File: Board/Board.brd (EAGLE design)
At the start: 99 x 99 mm, 108 parts, among them IC1 7805TV, IC2 LM358D, IC3 MCP23S17SO, IC4 ATMEGA328P_TQFP, IC5 MAX232SOIC16, IC6 MCP4921, IC7 TL431CD, IC8 DS18B20, IC9 DS18B20, Q1 IRF3710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

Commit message: renamed Board Files in preparation for Exporting PDFs
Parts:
- KK1, KK3: value SK104-PAD -> SK104
- KK2: value SK95-2M3 -> SK95
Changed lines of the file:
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@@
 <attribute name="VALUE" x="63.627" y="55.245" size="1.27" layer="27" rot="R90"/>
 </element>
-<element name="KK1" library="heatsink" package="SK104-PAD" value="SK104-PAD" x="91.44" y="68.58" smashed="yes" rot="R270">
+<element name="KK1" library="heatsink" package="SK104-PAD" value="SK104" x="91.44" y="68.58" smashed="yes" rot="R270">
 <attribute name="VALUE" x="84.963" y="75.184" size="1.778" layer="27" ratio="10" rot="R270"/>
 </element>
@@
 <attribute name="VALUE" x="30.48" y="49.53" size="0.4064" layer="27" rot="R180"/>
 </element>
-<element name="KK2" library="heatsink" package="SK95-2M3" value="SK95-2M3" x="6.35" y="71.12" smashed="yes" rot="R90">
+<element name="KK2" library="heatsink" package="SK95-2M3" value="SK95" x="6.35" y="71.12" smashed="yes" rot="R90">
 <attribute name="VALUE" x="0.635" y="71.12" size="1.27" layer="27" ratio="10" rot="R90"/>
 </element>
@@
 <element name="JP3" library="SparkFun-Connectors" package="MOLEX-1X4" value="" x="63.5" y="92.44" rot="MR270"/>
 <element name="JP4" library="SparkFun-Connectors" package="MOLEX-1X4" value="" x="25.4" y="57.15"/>
-<element name="KK3" library="heatsink" package="SK104-PAD" value="SK104-PAD" x="91.44" y="29.21" smashed="yes" rot="R270">
+<element name="KK3" library="heatsink" package="SK104-PAD" value="SK104" x="91.44" y="29.21" smashed="yes" rot="R270">
 <attribute name="VALUE" x="84.963" y="35.814" size="1.778" layer="27" ratio="10" rot="R270"/>
 </element>

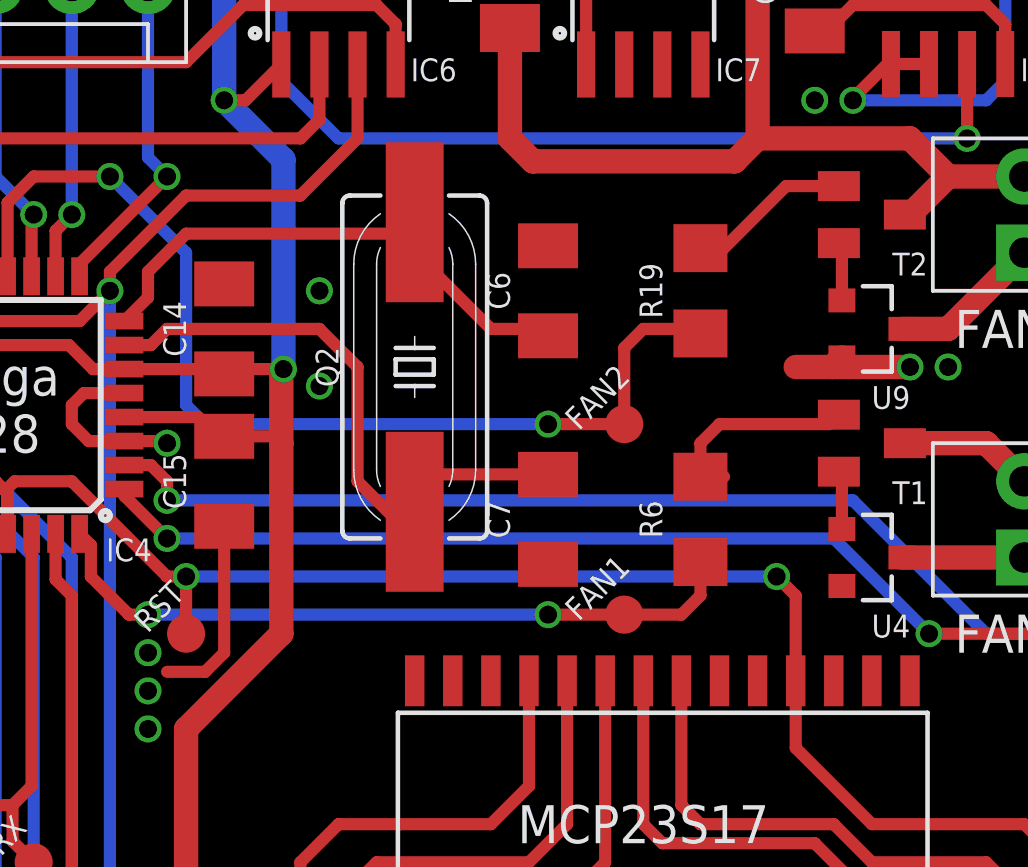
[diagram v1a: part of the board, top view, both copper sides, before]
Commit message: added pull downs to fan drver gates
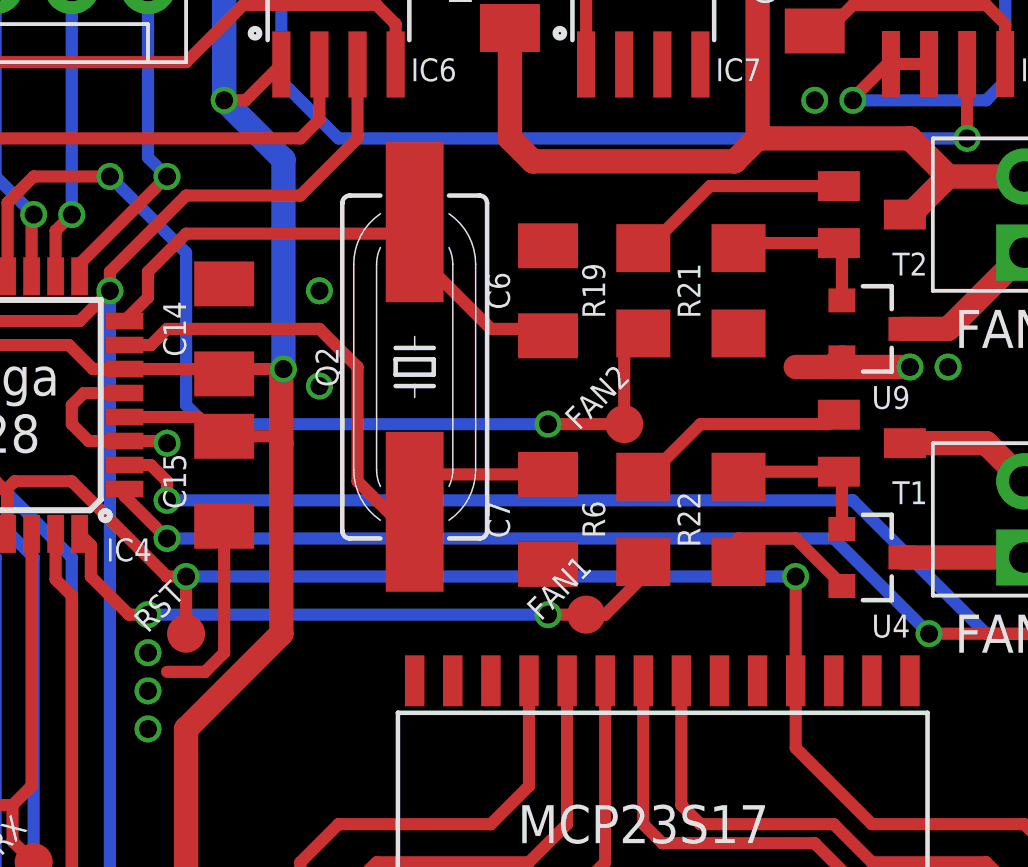
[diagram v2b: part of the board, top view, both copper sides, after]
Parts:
- added R21, R22: 10k, rcl:R1206
- moved R19 1.91 mm to (49.5, 47.0)
- moved R6 1.91 mm to (49.5, 39.4)
- moved FAN1 1.27 mm to (47.6, 36.2)
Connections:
- net GND: now also R21.2, R22.2
- net N$4: now also R22.1
- net N$42: now also R21.1
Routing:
- net GND: track 49.9 -> 54.8 mm
- net N$42: track 1.95 -> 5.37 mm
- net N$4: track 1.95 -> 5.37 mm
- net N$48: track 5.60 -> 8.60 mm
- net FAN1: track 23.8 -> 21.5 mm
- net FAN2: track 35.2 -> 34.2 mm

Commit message: lowered decoupling capacitance for VREF to allow fast switching of references
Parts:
- C18: value 100n -> 22p
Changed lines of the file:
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@@
 <attribute name="VALUE" x="81.28" y="71.12" size="1.27" layer="27" rot="R180"/>
 </element>
-<element name="C18" library="rcl" package="C1206K" value="100n" x="18.415" y="43.815" smashed="yes" rot="R180">
+<element name="C18" library="rcl" package="C1206K" value="22p" x="18.415" y="43.815" smashed="yes" rot="R180">
 <attribute name="NAME" x="18.415" y="45.085" size="0.762" layer="25" rot="R180" align="top-center"/>
 <attribute name="VALUE" x="20.015" y="45.915" size="1.016" layer="27" rot="R180"/>

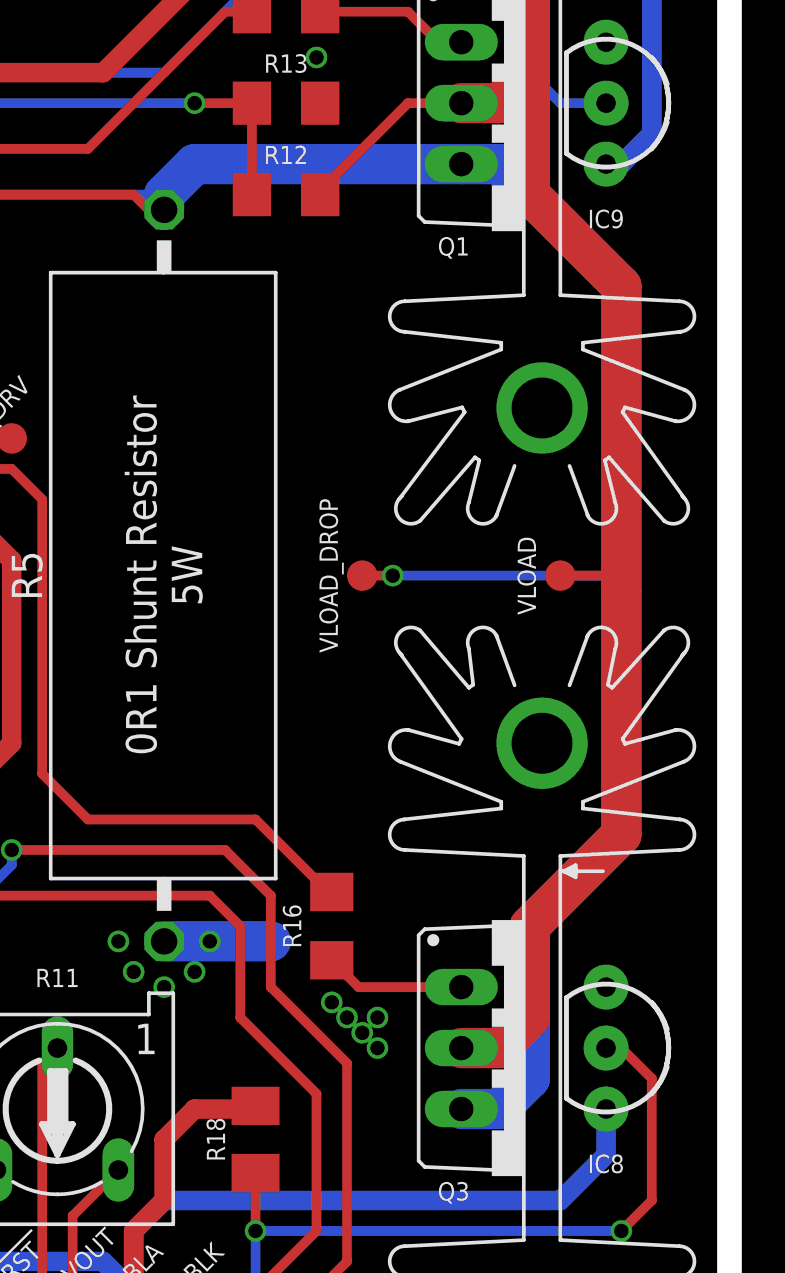
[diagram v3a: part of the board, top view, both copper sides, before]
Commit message: split out source path of the driving MosFETs
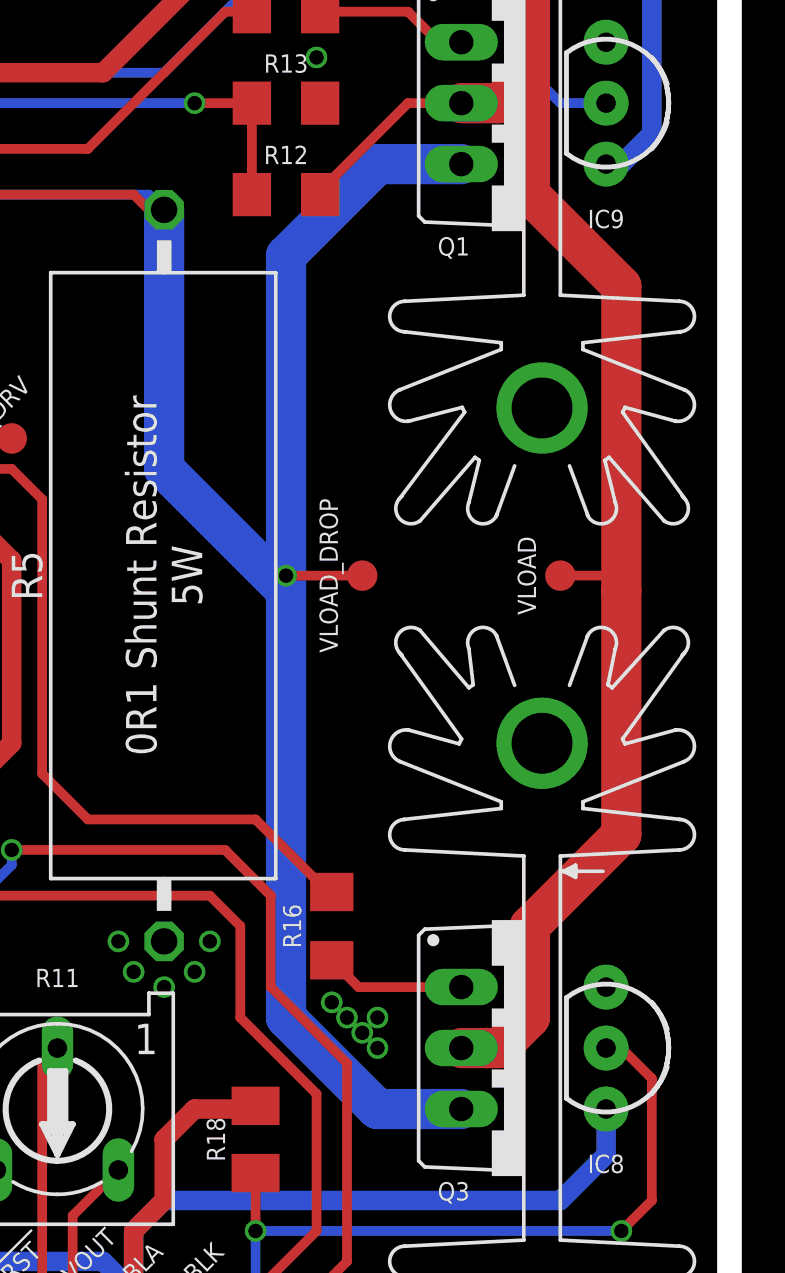
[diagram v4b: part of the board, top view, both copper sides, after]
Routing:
- net GND: track 54.8 -> 50.4 mm
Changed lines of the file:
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@@
 <via x="83.185" y="73.66" extent="1-16" drill="0.6" shape="octagon"/>
 <via x="84.455" y="73.66" extent="1-16" drill="0.6" shape="octagon"/>
-<wire x1="74.93" y1="33.655" x2="79.375" y2="33.655" width="1.6764" layer="16"/>
 <via x="82.55" y="30.48" extent="1-16" drill="0.6" shape="octagon"/>
 <via x="81.915" y="31.115" extent="1-16" drill="0.6" shape="octagon"/>
@@
 <contactref element="IC4" pad="25"/>
 <contactref element="Q3" pad="3"/>
-<wire x1="74.93" y1="64.135" x2="74.93" y2="64.77" width="1.6764" layer="16"/>
-<wire x1="74.93" y1="64.77" x2="76.2" y2="66.04" width="1.6764" layer="16"/>
-<wire x1="76.2" y1="66.04" x2="87.3125" y2="66.04" width="1.6764" layer="16"/>
 <wire x1="60.325" y1="59.75" x2="60.325" y2="64.135" width="0.4064" layer="1"/>
 <via x="24.13" y="37.465" extent="1-16" drill="0.6" shape="octagon"/>
@@
 <wire x1="64.135" y1="64.77" x2="64.287" y2="64.922" width="0.4064" layer="1"/>
 <wire x1="64.287" y1="64.922" x2="64.77" y2="64.922" width="0.4064" layer="1"/>
-<wire x1="87.3125" y1="26.67" x2="88.9" y2="26.67" width="1.6764" layer="16"/>
-<wire x1="88.9" y1="26.67" x2="90.17" y2="27.94" width="1.6764" layer="16"/>
-<wire x1="90.17" y1="27.94" x2="90.17" y2="34.29" width="1.6764" layer="16"/>
-<wire x1="90.17" y1="34.29" x2="93.98" y2="38.1" width="1.6764" layer="16"/>
-<wire x1="93.98" y1="38.1" x2="93.98" y2="48.895" width="1.6764" layer="16"/>
-<wire x1="93.98" y1="48.895" x2="93.98" y2="60.96" width="1.6764" layer="16"/>
-<wire x1="93.98" y1="60.96" x2="88.9" y2="66.04" width="1.6764" layer="16"/>
-<wire x1="88.9" y1="66.04" x2="87.3125" y2="66.04" width="1.6764" layer="16"/>
-<wire x1="93.98" y1="48.895" x2="84.455" y2="48.895" width="0.4064" layer="16"/>
-<via x="84.455" y="48.895" extent="1-16" drill="0.6" shape="octagon"/>
-<wire x1="84.455" y1="48.895" x2="83.185" y2="48.895" width="0.4064" layer="1"/>
 <wire x1="24.13" y1="37.465" x2="24.765" y2="38.1" width="0.4064" layer="1"/>
 <wire x1="24.765" y1="38.1" x2="24.765" y2="38.5124" width="0.4064" layer="1"/>
 <wire x1="24.765" y1="38.5124" x2="25.14" y2="38.8874" width="0.4064" layer="1"/>
+<wire x1="87.3125" y1="26.67" x2="83.82" y2="26.67" width="1.6764" layer="16"/>
+<wire x1="83.82" y1="26.67" x2="80.01" y2="30.48" width="1.6764" layer="16"/>
+<wire x1="80.01" y1="30.48" x2="80.01" y2="48.26" width="1.6764" layer="16"/>
+<wire x1="80.01" y1="48.26" x2="80.01" y2="48.895" width="1.6764" layer="16"/>
+<wire x1="83.185" y1="48.895" x2="80.01" y2="48.895" width="0.4064" layer="1"/>
+<via x="80.01" y="48.895" extent="1-16" drill="0.6" shape="octagon"/>
+<wire x1="87.3125" y1="66.04" x2="83.82" y2="66.04" width="1.6764" layer="16"/>
+<wire x1="83.82" y1="66.04" x2="80.01" y2="62.23" width="1.6764" layer="16"/>
+<wire x1="80.01" y1="62.23" x2="80.01" y2="48.895" width="1.6764" layer="16"/>
+<wire x1="74.93" y1="64.135" x2="74.93" y2="53.34" width="1.6764" layer="16"/>
+<wire x1="74.93" y1="53.34" x2="80.01" y2="48.26" width="1.6764" layer="16"/>
 </signal>
 <signal name="VREF_BUF">

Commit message: updated firmware
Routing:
- net N$14: track 31.2 -> 30.5 mm
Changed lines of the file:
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@@
 <?xml version="1.0" encoding="utf-8"?>
 <!DOCTYPE eagle SYSTEM "eagle.dtd">
-<eagle version="6.5.0">
+<eagle version="8.0.0">
 <drawing>
 <settings>
@@
 <pass name="Default">
 <param name="RoutingGrid" value="50mil"/>
+<param name="AutoGrid" value="1"/>
+<param name="Efforts" value="0"/>
+<param name="TopRouterVariant" value="1"/>
 <param name="tpViaShape" value="round"/>
 <param name="PrefDir.1" value="|"/>
@@
 <contactref element="C5" pad="2"/>
 <contactref element="IC2" pad="4"/>
-<contactref element="IC6" pad="7"/>
 <contactref element="IC6" pad="7"/>
 <contactref element="IC6" pad="5"/>
@@
 <wire x1="56.15" y1="40.86" x2="56.05" y2="40.96" width="0.4064" layer="1"/>
 <contactref element="R22" pad="1"/>
-<contactref element="R22" pad="1"/>
 <wire x1="56.05" y1="40.96" x2="52.873" y2="40.96" width="0.4064" layer="1"/>
 <wire x1="52.873" y1="40.96" x2="52.705" y2="40.792" width="0.4064" layer="1"/>
@@
 <wire x1="33.02" y1="8.89" x2="33.02" y2="11.43" width="0.4064" layer="1"/>
 <wire x1="33.02" y1="11.43" x2="31.75" y2="12.7" width="0.4064" layer="1"/>
-<wire x1="31.75" y1="12.7" x2="26.035" y2="12.7" width="0.4064" layer="1"/>
+<wire x1="24.765" y1="14.605" x2="24.765" y2="14.119903125" width="0.4064" layer="1"/>
+<wire x1="24.765" y1="14.119903125" x2="26.184903125" y2="12.7" width="0.4064" layer="1"/>
+<wire x1="26.184903125" y1="12.7" x2="31.75" y2="12.7" width="0.4064" layer="1"/>
 <wire x1="24.765" y1="20.955" x2="23.495" y2="22.225" width="0.4064" layer="1"/>
 <wire x1="23.495" y1="22.225" x2="16.25" y2="22.225" width="0.4064" layer="1"/>
@@
 <wire x1="29.21" y1="6.35" x2="29.21" y2="7.13" width="0.4064" layer="1"/>
 <wire x1="29.21" y1="7.13" x2="29.55" y2="7.47" width="0.4064" layer="1"/>
-<wire x1="26.035" y1="12.7" x2="24.765" y2="13.97" width="0.4064" layer="1"/>
 <wire x1="24.765" y1="14.605" x2="24.765" y2="20.955" width="0.4064" layer="1"/>
 <wire x1="24.13" y1="15.24" x2="24.765" y2="14.605" width="0.4064" layer="1"/>
-<wire x1="24.765" y1="14.605" x2="24.765" y2="13.97" width="0.4064" layer="1"/>
 </signal>
 <signal name="N$14">
@@
 <wire x1="15.24" y1="26.67" x2="11.43" y2="26.67" width="0.4064" layer="16"/>
 <via x="11.43" y="26.67" extent="1-16" drill="0.6" shape="octagon"/>
-<wire x1="25.4" y1="10.31" x2="25.4" y2="11.43" width="0.4064" layer="1"/>
-<wire x1="25.4" y1="11.43" x2="24.13" y2="12.7" width="0.4064" layer="1"/>
-<wire x1="24.13" y1="12.7" x2="17.78" y2="12.7" width="0.4064" layer="1"/>
+<wire x1="25.4" y1="10.31" x2="23.01" y2="12.7" width="0.4064" layer="1"/>
+<wire x1="23.01" y1="12.7" x2="17.78" y2="12.7" width="0.4064" layer="1"/>
 <wire x1="17.78" y1="12.7" x2="16.51" y2="13.97" width="0.4064" layer="1"/>
 <wire x1="16.51" y1="13.97" x2="16.51" y2="15.24" width="0.4064" layer="1"/>
@@
 <wire x1="56.15" y1="48.48" x2="56.05" y2="48.58" width="0.4064" layer="1"/>
 <contactref element="R21" pad="1"/>
-<contactref element="R21" pad="1"/>
 <wire x1="56.05" y1="48.58" x2="52.873" y2="48.58" width="0.4064" layer="1"/>
